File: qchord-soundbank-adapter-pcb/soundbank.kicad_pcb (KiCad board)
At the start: 2 copper layers, 16 x 29.7 mm, 2 parts, among them U1 8Mbit ROM, U2 8Mbit Flash

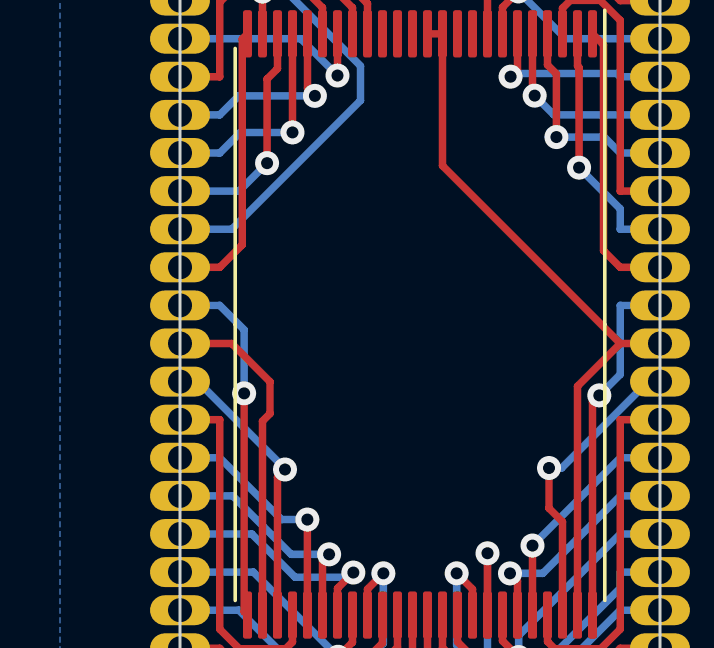
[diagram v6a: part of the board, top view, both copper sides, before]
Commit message: Adds some docs, pre-reversed Q616 dump
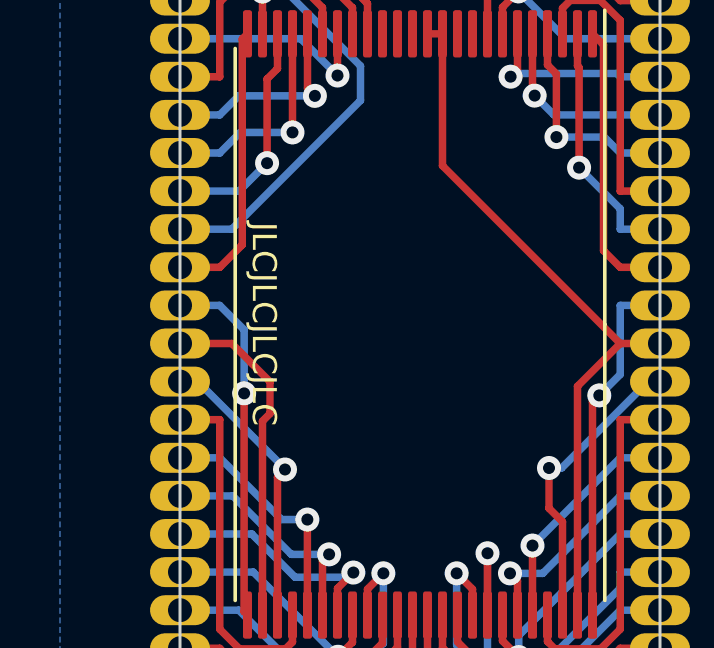
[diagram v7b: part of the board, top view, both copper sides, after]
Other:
- board text added: "JLCJLCJLCJLC"
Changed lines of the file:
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@@
     (effects (font (size 0.8 0.8) (thickness 0.1)) (justify bottom mirror))
+  )
+  (gr_text "JLCJLCJLCJLC" (at 89.3 77.4 270) (layer "F.SilkS")
+    (effects (font (size 0.8 0.8) (thickness 0.1)))
   )
   (gr_text "Q616" (at 94.5 91.1) (layer "F.SilkS")
